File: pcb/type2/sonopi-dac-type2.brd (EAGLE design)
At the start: 65 x 30 mm, 27 parts, among them J1 HLR-3201VXB-004HG, J2 HLR-3201VXB-003HG, J3 RASPI_BOARD_B+#_ZERO, U1 PCM5122PW, U2 MCP1703AT-3302E/CB, X1 22.5792MHz, X2 24.576MHz

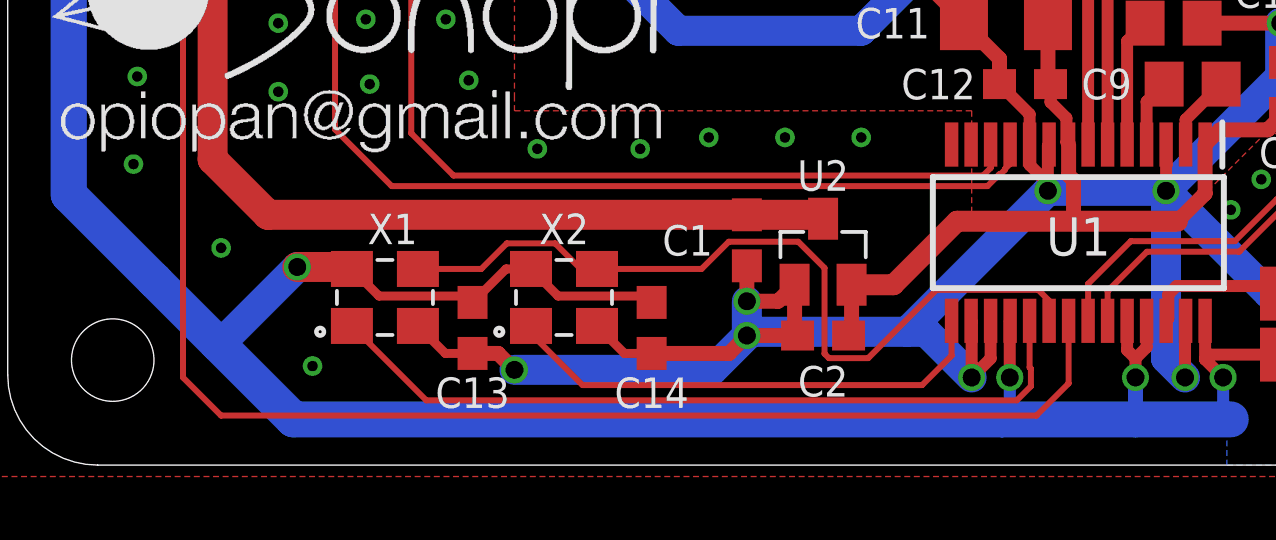
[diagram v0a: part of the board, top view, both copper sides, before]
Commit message: add panelizing script
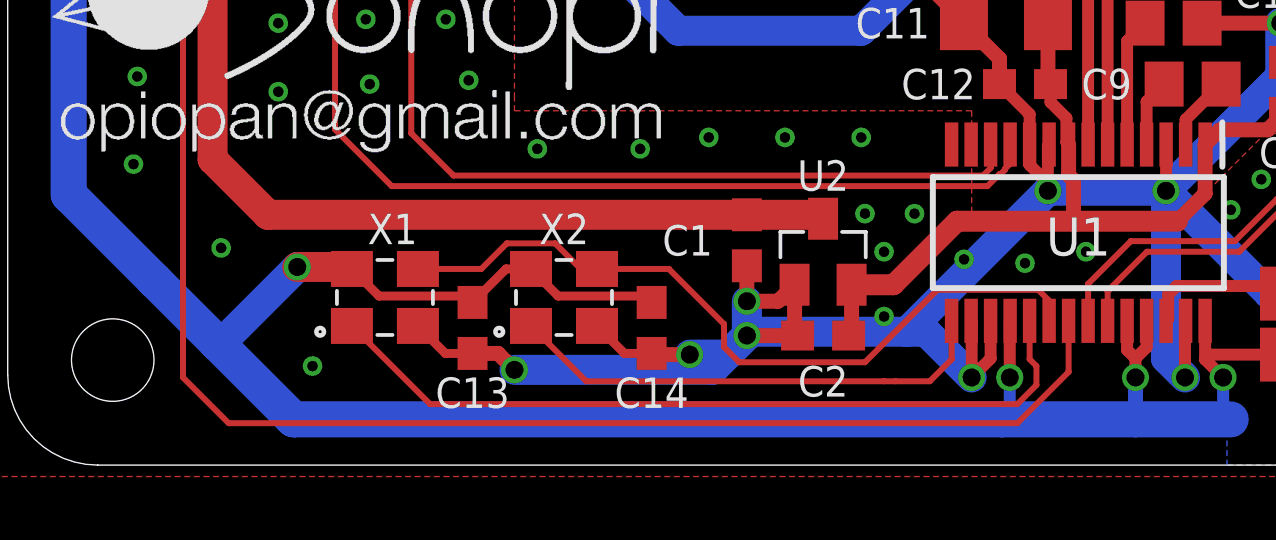
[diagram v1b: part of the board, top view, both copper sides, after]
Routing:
- net SCLK: track 27.2 -> 25.3 mm
- net GND: track 184.1 -> 184.2 mm, vias 66 -> 74
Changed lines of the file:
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@@
 </layers>
 <board>
-<fusionsync huburn="a.cGVyc29uYWw6dWUyYmE2M2My" projecturn="a.cGVyc29uYWw6dWUyYmE2M2MyIzIwMTgwOTE3MTQ5MTY5Mjgx" f3durn="urn:adsk.wipprod:dm.lineage:frYCqByTTnG5slPWVEB-oA" pcbguid="7cebb721-e281-4a90-b6c0-b829a01244c8" lastpulledtime="" lastsyncedchangeguid="46c38bd1-cc02-f853-66d1-19df69127135"/>
+<fusionsync huburn="a.cGVyc29uYWw6dWUyYmE2M2My" projecturn="a.cGVyc29uYWw6dWUyYmE2M2MyIzIwMTgwOTE3MTQ5MTY5Mjgx" f3durn="urn:adsk.wipprod:dm.lineage:sNxieVbiRFS_U6zmVQ5HhQ" pcbguid="cf84b80f-ad96-481d-989d-4a0cf6bf29d6" lastpulledtime="" lastsyncedchangeguid="52219b5c-18a8-7e58-fa47-0e398aab598c"/>
 <plain>
 <text x="58.547" y="1.397" size="1.4" layer="21" align="bottom-right">V1.0</text>
@@
 <attribute name="VALUE" x="34.544" y="14.605" size="1.27" layer="27" rot="R180"/>
 </element>
-<element name="J1" library="RCA-jack" library_urn="urn:adsk.eagle:library:15327963" package="HLR-3201VXB" package3d_urn="urn:adsk.eagle:package:15481381/2" value="HLR-3201VXB-004HG" x="44.831" y="30" smashed="yes" rot="R180">
+<element name="J1" library="RCA-jack" library_urn="urn:adsk.eagle:library:15327963" package="HLR-3201VXB" package3d_urn="urn:adsk.eagle:package:15481381/4" value="HLR-3201VXB-004HG" x="44.831" y="30" smashed="yes" rot="R180">
 <attribute name="NAME" x="44.831" y="22.38" size="1.27" layer="25" rot="R180" align="bottom-center"/>
 </element>
-<element name="J2" library="RCA-jack" library_urn="urn:adsk.eagle:library:15327963" package="HLR-3201VXB" package3d_urn="urn:adsk.eagle:package:15481381/2" value="HLR-3201VXB-003HG" x="27.813" y="30" smashed="yes" rot="R180">
+<element name="J2" library="RCA-jack" library_urn="urn:adsk.eagle:library:15327963" package="HLR-3201VXB" package3d_urn="urn:adsk.eagle:package:15481381/4" value="HLR-3201VXB-003HG" x="27.813" y="30" smashed="yes" rot="R180">
 <attribute name="NAME" x="27.813" y="22.38" size="1.27" layer="25" rot="R180" align="bottom-center"/>
 </element>
@@
 <wire x1="32.762" y1="4.809" x2="32.762" y2="3.552" width="0.4" layer="1"/>
 <wire x1="32.762" y1="3.552" x2="32.131" y2="2.921" width="0.4" layer="1"/>
-<wire x1="24.638" y1="4.318" x2="24.042" y2="3.722" width="0.5" layer="1"/>
-<wire x1="24.042" y1="3.722" x2="21.463" y2="3.722" width="0.5" layer="1"/>
 <via x="16.891" y="3.175" extent="1-16" drill="0.6"/>
 <wire x1="15.494" y1="3.722" x2="16.344" y2="3.722" width="0.5" layer="1"/>
@@
 <via x="52.832" y="3.683" extent="1-16" drill="0.35"/>
 <via x="50.292" y="3.683" extent="1-16" drill="0.35"/>
+<via x="22.733" y="3.683" extent="1-16" drill="0.6"/>
+<wire x1="22.733" y1="3.683" x2="24.003" y2="3.683" width="1" layer="16"/>
+<wire x1="24.003" y1="3.683" x2="24.638" y2="4.318" width="1" layer="16"/>
+<wire x1="22.733" y1="3.683" x2="21.502" y2="3.683" width="0.5" layer="1"/>
+<wire x1="21.502" y1="3.683" x2="21.463" y2="3.722" width="0.5" layer="1"/>
+<via x="28.575" y="8.382" extent="1-16" drill="0.35"/>
+<via x="30.226" y="8.382" extent="1-16" drill="0.35"/>
+<via x="29.21" y="7.112" extent="1-16" drill="0.35"/>
+<via x="31.877" y="6.858" extent="1-16" drill="0.35"/>
+<via x="33.909" y="6.731" extent="1-16" drill="0.35"/>
+<via x="29.21" y="4.953" extent="1-16" drill="0.35"/>
+<via x="35.941" y="7.112" extent="1-16" drill="0.35"/>
 </signal>
 <signal name="+3V3/A">
@@
 <wire x1="21.07" y1="27.77" x2="19.757" y2="29.083" width="0.2" layer="1"/>
 <wire x1="8.0688125" y1="29.083" x2="5.842" y2="26.8561875" width="0.2" layer="1"/>
-<wire x1="5.842" y1="2.921" x2="7.112" y2="1.651" width="0.2" layer="1"/>
-<wire x1="7.112" y1="1.651" x2="34.29" y2="1.651" width="0.2" layer="1"/>
-<wire x1="35.362" y1="2.723" x2="35.362" y2="4.809" width="0.2" layer="1"/>
 <wire x1="19.757" y1="29.083" x2="8.0688125" y2="29.083" width="0.2" layer="1"/>
 <wire x1="5.842" y1="26.8561875" x2="5.842" y2="2.921" width="0.2" layer="1"/>
-<wire x1="34.29" y1="1.651" x2="35.362" y2="2.723" width="0.2" layer="1"/>
+<wire x1="5.842" y1="2.921" x2="7.366" y2="1.397" width="0.2" layer="1"/>
+<wire x1="35.362" y1="3.104" x2="35.362" y2="4.809" width="0.2" layer="1"/>
+<wire x1="7.366" y1="1.397" x2="33.655" y2="1.397" width="0.2" layer="1"/>
+<wire x1="33.655" y1="1.397" x2="35.362" y2="3.104" width="0.2" layer="1"/>
 </signal>
 <signal name="LRCLK">
@@
 <wire x1="15.78505" y1="6.538" x2="16.63745" y2="7.3904" width="0.2" layer="1"/>
 <wire x1="18.24655" y1="7.3904" x2="19.09895" y2="6.538" width="0.2" layer="1"/>
-<wire x1="27.2256" y1="3.71345" x2="27.37345" y2="3.5656" width="0.2" layer="1"/>
-<wire x1="27.37345" y1="3.5656" x2="28.68255" y2="3.5656" width="0.2" layer="1"/>
-<wire x1="19.642" y1="6.538" x2="23.12605" y2="6.538" width="0.2" layer="1"/>
-<wire x1="23.12605" y1="6.538" x2="24.03345" y2="7.4454" width="0.2" layer="1"/>
-<wire x1="27.2256" y1="6.57135" x2="27.2256" y2="3.71345" width="0.2" layer="1"/>
-<wire x1="24.03345" y1="7.4454" x2="26.35155" y2="7.4454" width="0.2" layer="1"/>
-<wire x1="26.35155" y1="7.4454" x2="27.2256" y2="6.57135" width="0.2" layer="1"/>
-<wire x1="28.68255" y1="3.5656" x2="30.95895" y2="5.842" width="0.2" layer="1"/>
 <wire x1="34.34845" y1="5.842" x2="34.712" y2="5.47845" width="0.2" layer="1"/>
 <wire x1="34.712" y1="5.47845" x2="34.712" y2="4.809" width="0.2" layer="1"/>
-<wire x1="30.95895" y1="5.842" x2="34.34845" y2="5.842" width="0.2" layer="1"/>
+<wire x1="30.95895" y1="5.842" x2="30.988" y2="5.842" width="0.2" layer="1"/>
+<wire x1="30.988" y1="5.842" x2="34.34845" y2="5.842" width="0.2" layer="1"/>
+<wire x1="19.642" y1="6.538" x2="22.037" y2="6.538" width="0.2" layer="1"/>
+<wire x1="22.037" y1="6.538" x2="23.876" y2="4.699" width="0.2" layer="1"/>
+<wire x1="23.876" y1="4.699" x2="23.876" y2="3.937" width="0.2" layer="1"/>
+<wire x1="23.876" y1="3.937" x2="24.384" y2="3.429" width="0.2" layer="1"/>
+<wire x1="28.575" y1="3.429" x2="30.988" y2="5.842" width="0.2" layer="1"/>
+<wire x1="24.384" y1="3.429" x2="28.575" y2="3.429" width="0.2" layer="1"/>
 </signal>
 <signal name="EN48">
 <contactref element="U1" pad="15"/>
 <contactref element="X2" pad="1"/>
-<wire x1="31.462" y1="4.809" x2="31.462" y2="3.649" width="0.2" layer="1"/>
-<wire x1="31.462" y1="3.649" x2="30.48" y2="2.667" width="0.2" layer="1"/>
-<wire x1="30.48" y1="2.667" x2="19.159" y2="2.667" width="0.2" layer="1"/>
-<wire x1="19.159" y1="2.667" x2="17.442" y2="4.384" width="0.2" layer="1"/>
 <wire x1="17.442" y1="4.384" x2="17.442" y2="4.638" width="0.2" layer="1"/>
+<wire x1="17.442" y1="4.638" x2="19.286" y2="2.794" width="0.2" layer="1"/>
+<wire x1="19.286" y1="2.794" x2="29.21" y2="2.794" width="0.2" layer="1"/>
+<wire x1="29.21" y1="2.794" x2="29.591" y2="2.794" width="0.2" layer="1"/>
+<wire x1="29.591" y1="2.794" x2="30.734" y2="2.794" width="0.2" layer="1"/>
+<wire x1="31.462" y1="3.522" x2="31.462" y2="4.809" width="0.2" layer="1"/>
+<wire x1="30.734" y1="2.794" x2="31.462" y2="3.522" width="0.2" layer="1"/>
 </signal>
 <signal name="LDOO">
@@
 <contactref element="X1" pad="1"/>
 <contactref element="U1" pad="19"/>
-<wire x1="34.1058" y1="3.21294375" x2="34.1058" y2="2.62905625" width="0.2" layer="1"/>
-<wire x1="34.1058" y1="2.62905625" x2="33.63574375" y2="2.159" width="0.2" layer="1"/>
-<wire x1="34.062" y1="4.809" x2="34.062" y2="3.25674375" width="0.2" layer="1"/>
-<wire x1="34.062" y1="3.25674375" x2="34.1058" y2="3.21294375" width="0.2" layer="1"/>
-<wire x1="13.952" y1="2.159" x2="33.63574375" y2="2.159" width="0.2" layer="1"/>
-<wire x1="11.473" y1="4.638" x2="13.952" y2="2.159" width="0.2" layer="1"/>
+<wire x1="11.473" y1="4.638" x2="14.079" y2="2.032" width="0.2" layer="1"/>
+<wire x1="33.655" y1="2.032" x2="34.29" y2="2.667" width="0.2" layer="1"/>
+<wire x1="34.29" y1="2.667" x2="34.29" y2="3.302" width="0.2" layer="1"/>
+<wire x1="34.062" y1="3.53" x2="34.062" y2="4.809" width="0.2" layer="1"/>
+<wire x1="14.079" y1="2.032" x2="33.655" y2="2.032" width="0.2" layer="1"/>
+<wire x1="34.29" y1="3.302" x2="34.062" y2="3.53" width="0.2" layer="1"/>
 </signal>
 </signals>

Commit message: change footprint of 3225 oscillator
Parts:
- X1, X2: device oscillator:3225-SMD -> oscillator:3225-SMD-HS
- moved X1 2.67 mm to (9.91, 5.59)
- moved C13 1.90 mm to (13.6, 4.57)
- moved X2 0.76 mm to (17.8, 5.59)
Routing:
- net GND: track 184.2 -> 187.4 mm, vias 74 -> 72
- net +3V3: track 96.1 -> 99.1 mm
- net EN44: track 26.4 -> 29.3 mm
- net SCLK: track 25.3 -> 27.7 mm
- net EN48: track 16.6 -> 17.7 mm
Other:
- board text added: "V1.1"
- board text removed: "V1.0"
